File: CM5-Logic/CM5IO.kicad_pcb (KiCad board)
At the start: 4 copper layers, 165 x 165 mm, 129 parts, among them J1 703W-00_53, J10 691210910004, J11 690-019-298-412, J12 USB3_A, J13 JST_SHBM04B-SRSS-TB, J14 Micro_SD_Card_Det, J15 Bus_M.2_Socket_M, J16 SSW-114-01-X-S, J17 SSW-114-01-X-S, J18 6130XX11821_61300811821, J19 6130XX11821_61300811821, J2 B2B-PH-K-S, J20 6130XX11821_61300811821, J21 6130XX11821_61300811821, J3 B2B-PH-K-S, J4 VR10S09, J5 691101810005, J6 691210910006, J7 691210910006, J8 5055750471, J9 1726470103, U1 UWS-5_10-Q48N-C, U10 AP3441SHE-7B, U11 ASEK-32.768KHZ-L-R-T, U12 MAX98357AETE_T, U13 MAX98357AETE_T, U14 CDCLVC1106PWR, U15 CDCLVC1106PWR, U2 RCLAMP3354S.TCT, U3 AP22653W6, U4 RT9742SNGV, U5 74LVC1G07SE-7, U6 TPD4EUSB30, U7 TPD4EUSB30, U8 RT9742GGJ5, U9 MagJack-A70-112-331N126

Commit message: changes USB port, adds TMC2209 SilentStepStick footprint, redoes PCB Layout
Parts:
- removed C35: 10uF, PCM_JLCPCB:C_0402
- removed C36, C37: 100nF, PCM_JLCPCB:C_0402
- removed F1: 4628, Custom Components:FUSE_4628
- removed H1, H2, H3, H4, H5, H6, H7, H8: MountingHole, CM5IO:MountingHole_2.7mm_M2.5_DIN965
- removed J19, J20, J21: 6130XX11821_61300811821, Custom Components:61300811821
- removed MK1, MK2, MK3, MK4, MK5, MK6, MK7, MK8: ICS-43434, Sensor_Audio:InvenSense_ICS-43434-6_3.5x2.65mm
- removed R15, R16, R17, R18, R19, R20: 100Ω, PCM_JLCPCB:R_0603
- removed R21: 2.2kΩ, PCM_JLCPCB:R_0402
- removed R22: 100kΩ, PCM_JLCPCB:R_0402
- removed R23, R24, R25, R26, R27, R28, R29, R30, R31, R32: 33Ω, PCM_JLCPCB:R_0402
- removed U12, U13: MAX98357AETE_T, Custom Components:QFN50P300X300X80-17N
- removed U14, U15: CDCLVC1106PWR, Custom Components:SOP65P640X120-14N
- added PS1: R-78E9.0-0.5, Custom Components:CONV_R-78E9.0-0.5, F.Cu at (535.2, 244.7)
- C10, C24: footprint PCM_JLCPCB:C_0402 -> PCM_JLCPCB:C_0603
- C11, C25, C30: value 100nF -> 10uF; footprint PCM_JLCPCB:C_0402 -> PCM_JLCPCB:C_0805
- C12, C8: value 10uF -> 100nF; footprint PCM_JLCPCB:C_0805 -> PCM_JLCPCB:C_0402
- C13: value 100nF -> 10uF; footprint PCM_JLCPCB:C_0402 -> PCM_JLCPCB:C_0805; moved to B.Cu
- C14, C18, C19, C20, D3, L1, Module1, TP1: moved to B.Cu
- C15, C21: value 10uF -> 100nF; footprint PCM_JLCPCB:C_0805 -> PCM_JLCPCB:C_0402; moved to B.Cu
- C16: value 100nF -> 4.7nF; moved to B.Cu
- C17: value 4.7nF -> 10uF; footprint PCM_JLCPCB:C_0402 -> PCM_JLCPCB:C_0805; moved to B.Cu
- C2: value 22uF -> 10uF; footprint PCM_JLCPCB:C_0805 -> PCM_JLCPCB:C_1206
- C22: value 100nF -> 10uF; footprint PCM_JLCPCB:C_0402 -> PCM_JLCPCB:C_CASE-A-3216-18(mm)
- C23: value WCAP-ASLI_6.3X7.7 -> 100nF; footprint Custom Components:WCAP-ASLI_6.3X7.7_DXL_ -> PCM_JLCPCB:C_0603
- C27: value 100nF -> WCAP-ASLI_6.3X7.7; footprint PCM_JLCPCB:C_0402 -> Custom Components:WCAP-ASLI_6.3X7.7_DXL_
- C3: value WCAP-FTX2_P22.5_CS -> 10uF; footprint Custom Components:WCAP-FTX2_P22.5L26W6H12_CS -> PCM_JLCPCB:C_0805
- C32, C33: value 10uF -> 100nF
- C34: footprint PCM_JLCPCB:C_0402 -> PCM_JLCPCB:C_0805
- C4: value DE1E3RA472MA4BN01F -> 100nF; footprint Custom Components:CAP_DE1E3RA472MA4BN01F -> PCM_JLCPCB:C_CASE-B-3528-21(mm)
- C5: value DE1E3RA472MA4BN01F -> 10uF; footprint Custom Components:CAP_DE1E3RA472MA4BN01F -> PCM_JLCPCB:C_0805
- C7: footprint PCM_JLCPCB:C_CASE-B-3528-21(mm) -> PCM_JLCPCB:C_0402
- C9: footprint PCM_JLCPCB:C_0805 -> PCM_JLCPCB:C_1206
- J1: value 703W-00_53 -> B2B-PH-K-S; footprint Custom Components:QUALTEK_703W-00_53 -> Custom Components:JST_B2B-PH-K-S
- J10: value 691210910004 -> JST_SHBM04B-SRSS-TB; footprint Custom Components:691210910004 -> Connector_JST:JST_SH_BM04B-SRSS-TB_1x04-1MP_P1.00mm_Vertical
- J11: value 690-019-298-412 -> Micro_SD_Card_Det; footprint CM5IO:EDAC 690-019-298-412 -> CM5IO:SDCARD_MOLEX_503398-1892; moved to B.Cu
- J12: value USB3_A -> Bus_M.2_Socket_M; footprint CM5IO:MTCONN_UBAF30-D2011 -> CM5IO:M.2 M Key socket; moved to B.Cu
- J13: value JST_SHBM04B-SRSS-TB -> 6130XX11821_61300811821; footprint Connector_JST:JST_SH_BM04B-SRSS-TB_1x04-1MP_P1.00mm_Vertical -> Custom Components:61300811821
- J14: value Micro_SD_Card_Det -> 6130XX11821_61300811821; footprint CM5IO:SDCARD_MOLEX_503398-1892 -> Custom Components:61300811821
- J15: value Bus_M.2_Socket_M -> SSW-120-01-G-S-LL; footprint CM5IO:M.2 M Key socket -> Custom Components:SAMTEC_SSW-120-01-G-S-LL
- J16: value SSW-114-01-X-S -> SSW-120-01-G-S-LL; footprint Custom Components:SAMTEC_SSW-114-01-X-S -> Custom Components:SAMTEC_SSW-120-01-G-S-LL
- J17: value SSW-114-01-X-S -> 63453-116LF; footprint Custom Components:SAMTEC_SSW-114-01-X-S -> Custom Components:AMPHENOL_63453-116LF
- J18: value 6130XX11821_61300811821 -> 63453-116LF; footprint Custom Components:61300811821 -> Custom Components:AMPHENOL_63453-116LF
- J3: value B2B-PH-K-S -> ED555/4DS; footprint Custom Components:JST_B2B-PH-K-S -> Custom Components:CONN4_ED555&slash_4DS_SHT
- J4: value VR10S09 -> 691210910006; footprint Custom Components:VR10S09 -> Custom Components:691210910006
- J5: value 691101810005 -> 691210910006; footprint Custom Components:691101810005 -> Custom Components:691210910006
- J6: value 691210910006 -> 39291247; footprint Custom Components:691210910006 -> Custom Components:CONN_SD-5569-002_24_MOL
- J7: value 691210910006 -> 39291087; footprint Custom Components:691210910006 -> Custom Components:CONN_SD-5569-002_08_MOL
- J8: value 5055750471 -> 690-019-298-412; footprint Custom Components:MOLEX_5055750471 -> CM5IO:EDAC 690-019-298-412; moved to B.Cu
- J9: value 1726470103 -> 484050003; footprint Custom Components:MOLEX_1726470103 -> Custom Components:484050003_MOL; moved to B.Cu
- R10: value 10kΩ -> 1kΩ; moved to B.Cu
- R11: value 2.2kΩ -> 5.1kΩ; footprint PCM_JLCPCB:R_0402 -> PCM_JLCPCB:R_0603
- R12: value 1kΩ -> 5.1kΩ; footprint PCM_JLCPCB:R_0402 -> PCM_JLCPCB:R_0603
- R13: value 100Ω -> 1MΩ
- R14: value 100Ω -> 470Ω
- R2: value 7.5kΩ -> 1kΩ
- R3: value 7.5kΩ -> 13kΩ; footprint PCM_JLCPCB:R_0402 -> PCM_JLCPCB:R_0805
- R5: value 13kΩ -> 470Ω; footprint PCM_JLCPCB:R_0805 -> PCM_JLCPCB:R_0402
- R6: value 1kΩ -> 470Ω
- R7: value 470Ω -> 100kΩ; moved to B.Cu
- R8: value 470Ω -> 10kΩ; moved to B.Cu
- R9: value 100kΩ -> 2.2kΩ; moved to B.Cu
- U1: value UWS-5_10-Q48N-C -> AP22653W6; footprint Custom Components:VREG_UWS-5_10-Q48N-C -> Package_TO_SOT_SMD:SOT-23-6; moved to F.Cu
- U10: value AP3441SHE-7B -> TMC2209_SILENTSTEPSTICK; footprint Package_DFN_QFN:DFN-8-1EP_2x2mm_P0.5mm_EP1.05x1.75mm -> Custom Components:MODULE_TMC2209_SILENTSTEPSTICK
- U11: value ASEK-32.768KHZ-L-R-T -> PAM8406DR; footprint Crystal:Crystal_SMD_3225-4Pin_3.2x2.5mm -> Custom Components:SO-16_PAM8406_DIO
- U2: value RCLAMP3354S.TCT -> RT9742SNGV; footprint Custom Components:SOT-23-5L_SEM -> Package_TO_SOT_SMD:TSOT-23_HandSoldering
- U3: value AP22653W6 -> 74LVC1G07SE-7; footprint Package_TO_SOT_SMD:SOT-23-6 -> Package_TO_SOT_SMD:SOT-353_SC-70-5
- U4: value RT9742SNGV -> TPD4EUSB30; footprint Package_TO_SOT_SMD:TSOT-23_HandSoldering -> Package_SON:USON-10_2.5x1.0mm_P0.5mm
- U5: value 74LVC1G07SE-7 -> TPD4EUSB30; footprint Package_TO_SOT_SMD:SOT-353_SC-70-5 -> Package_SON:USON-10_2.5x1.0mm_P0.5mm
- U6: value TPD4EUSB30 -> RT9742GGJ5; footprint Package_SON:USON-10_2.5x1.0mm_P0.5mm -> Package_TO_SOT_SMD:SOT-23-5
- U7: value TPD4EUSB30 -> MagJack-A70-112-331N126; footprint Package_SON:USON-10_2.5x1.0mm_P0.5mm -> CM5IO:TRJG0926HENL; moved to B.Cu
- U8: value RT9742GGJ5 -> AP3441SHE-7B; footprint Package_TO_SOT_SMD:SOT-23-5 -> Package_DFN_QFN:DFN-8-1EP_2x2mm_P0.5mm_EP1.05x1.75mm; moved to B.Cu
- U9: value MagJack-A70-112-331N126 -> ASEK-32.768KHZ-L-R-T; footprint CM5IO:TRJG0926HENL -> Crystal:Crystal_SMD_3225-4Pin_3.2x2.5mm; moved to B.Cu
- Ue1: value L9110S -> L9110H
- moved J1 382.3 mm to (335.4, 197.2), turned to 0 degrees
- moved C31 371.9 mm to (360.1, 180.3), turned to 0 degrees
- moved C23 367.4 mm to (290.3, 296.9), turned to 0 degrees
- moved C29 361.1 mm to (360.1, 176.6), turned to 0 degrees
- moved C3 360.3 mm to (328.1, 265.4), turned to 0 degrees
- moved R14 347.8 mm to (286.5, 298.2), turned to 0 degrees
- moved C5 340.1 mm to (328.1, 268.4)
- moved C1 336.1 mm to (334.5, 218.9), turned to 0 degrees
- moved D1 328.8 mm to (347.8, 250.8), turned to 0 degrees
- moved C4 327.0 mm to (340.3, 266.0), turned to 0 degrees
- moved D2 326.8 mm to (347.8, 253.4), turned to 0 degrees
- moved J10 317.7 mm to (372.6, 245.5), turned to 0 degrees
- moved C24 315.5 mm to (290.3, 299.1), turned to 0 degrees
- moved R13 314.8 mm to (286.5, 300.5), turned to 0 degrees
- moved R4 311.5 mm to (366.8, 247.0), turned to 0 degrees
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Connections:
- C1 pad 1: GND -> /+12v
- C1 pad 2: /+24v -> GND
- C11 pad 1: /CM5_HighSpeed/HDMI_5v -> /CM5_GPIO ( Ethernet, GPIO, SDCARD)/SD_PWR
- C12 pad 1: /CM5_GPIO ( Ethernet, GPIO, SDCARD)/SD_PWR -> Net-(C12-Pad1)
- C13 pad 1: Net-(C13-Pad1) -> /+5v
- C16 pad 1: /+5v -> /PCIe-M2/M2_3v3
- C16 pad 2: GND -> /PCIe-M2/FB
- C17 pad 2: /PCIe-M2/FB -> GND
- C22 pad 1: /PCIe-M2/M2_3v3 -> /+5v
- C23 pad 1: /+24v -> /+5v
- C24 pad 2: /+3.3v_P -> Net-(C24-Pad2)
- C25 pad 2: /+3.3v_P -> /+5v
- C26 pad 2: /+3.3v_P -> /+5v
- C27 pad 1: GND -> /+12v
- C27 pad 2: /+3.3v_P -> GND
- C28 pad 1: GND -> /+5v
- C28 pad 2: /+3.3v_P -> GND
- C29 pad 1: GND -> /+5v
- C29 pad 2: /+3.3v_P -> GND
- C3 pad 1: /AC_neutral2 -> /+5v
- C3 pad 2: /AC_line -> GND
- C30 pad 1: GND -> /+5v
- C30 pad 2: /+3.3v_P -> GND
- C31 pad 1: GND -> Net-(U11-INL)
- C31 pad 2: /+3.3v_P -> /HPL
- C32 pad 1: GND -> /HPR
- C32 pad 2: /+5v -> Net-(U11-INR)
- C33 pad 1: GND -> /+5v
- C33 pad 2: /+5v -> GND
- C34 pad 1: GND -> /+5v
- C34 pad 2: /+5v -> GND
- C4 pad 1: /AC_neutral2 -> /CM5_HighSpeed/VBUS
- C4 pad 2: /AC_Earth -> GND
- C5 pad 1: /AC_Earth -> /CM5_HighSpeed/VBUS
- C5 pad 2: /AC_line -> GND
- C6 pad 1: /+5v -> /CM5_HighSpeed/VBUS
- C7 pad 1: /CM5_HighSpeed/VBUS -> /+5v
- C8 pad 1: /CM5_HighSpeed/VBUS -> /CM5_HighSpeed/HDMI_5v
- C9 pad 1: /CM5_HighSpeed/VBUS -> /+5v
- D1 pad 2: /+3.3v_P -> /CM5_GPIO ( Ethernet, GPIO, SDCARD)/+3.3v_P
- D2 pad 2: /+3.3v_P -> /CM5_GPIO ( Ethernet, GPIO, SDCARD)/+3.3v_P
- J1 pad 1: /AC_neutral1 -> /PAM8406DR_Amp/OUT_R+
- J1 pad 2: /AC_Earth -> /PAM8406DR_Amp/OUT_R-
- J10 pad 1: /DRV225/S_B2 -> /+5v
- J10 pad 2: /DRV225/S_B1 -> /CM5_GPIO ( Ethernet, GPIO, SDCARD)/PWM
- J10 pad 3: /DRV225/S_A1 -> GND
- J10 pad 4: /DRV225/S_A2 -> /CM5_GPIO ( Ethernet, GPIO, SDCARD)/TACHO
- J11 pad 1: /CM5_HighSpeed/HDMI0_D2_P -> /CM5_GPIO ( Ethernet, GPIO, SDCARD)/SD_DAT2
- J11 pad 10: /CM5_HighSpeed/HDMI0_CK_P -> unconnected-(J11-DET_A-Pad10)
- J11 pad 2: GND -> /CM5_GPIO ( Ethernet, GPIO, SDCARD)/SD_DAT3
- J11 pad 3: /CM5_HighSpeed/HDMI0_D2_N -> /CM5_GPIO ( Ethernet, GPIO, SDCARD)/SD_CMD
- J11 pad 4: /CM5_HighSpeed/HDMI0_D1_P -> /CM5_GPIO ( Ethernet, GPIO, SDCARD)/SD_PWR
- J11 pad 5: GND -> /CM5_GPIO ( Ethernet, GPIO, SDCARD)/SD_CLK
- J11 pad 6: /CM5_HighSpeed/HDMI0_D1_N -> GND
- J11 pad 7: /CM5_HighSpeed/HDMI0_D0_P -> /CM5_GPIO ( Ethernet, GPIO, SDCARD)/SD_DAT0
- J11 pad 8: GND -> /CM5_GPIO ( Ethernet, GPIO, SDCARD)/SD_DAT1
- J11 pad 9: /CM5_HighSpeed/HDMI0_D0_N -> unconnected-(J11-DET_B-Pad9)
- J12 pad 10: GND -> Net-(J12-DAS/~{DSS}/~{LED1})
- J13 pad 1: /+5v -> GND
- J13 pad 2: /CM5_GPIO ( Ethernet, GPIO, SDCARD)/PWM -> GND
- J13 pad 4: /CM5_GPIO ( Ethernet, GPIO, SDCARD)/TACHO -> /+3.3v_ESP32
- J14 pad 1: /CM5_GPIO ( Ethernet, GPIO, SDCARD)/SD_DAT2 -> GND
- J14 pad 2: /CM5_GPIO ( Ethernet, GPIO, SDCARD)/SD_DAT3 -> /+3.3v_ESP32
- J14 pad 3: /CM5_GPIO ( Ethernet, GPIO, SDCARD)/SD_CMD -> /BNO086/SCK
- J14 pad 4: /CM5_GPIO ( Ethernet, GPIO, SDCARD)/SD_PWR -> /BNO086/SO
- J14 pad 5: /CM5_GPIO ( Ethernet, GPIO, SDCARD)/SD_CLK -> /BNO086/SI
- J14 pad 6: GND -> /BNO086/CS
- J14 pad 7: /CM5_GPIO ( Ethernet, GPIO, SDCARD)/SD_DAT0 -> /BNO086/WAK
- J14 pad 8: /CM5_GPIO ( Ethernet, GPIO, SDCARD)/SD_DAT1 -> unconnected-(J14-Pad8)
- J15 pad 10: Net-(J15-DAS/~{DSS}/~{LED1}) -> unconnected-(J15-Pad10)
- J15 pad 12: /PCIe-M2/M2_3v3 -> unconnected-(J15-Pad12)
- J15 pad 13: unconnected-(J15-PERp3-Pad13) -> /n_IA
- J15 pad 14: /PCIe-M2/M2_3v3 -> /n_IB
- J15 pad 15: GND -> /n_SenseSCL
- J15 pad 16: /PCIe-M2/M2_3v3 -> /n_SenseSDA
- J15 pad 17: unconnected-(J15-PETn2-Pad17) -> /n_RST
- J15 pad 18: /PCIe-M2/M2_3v3 -> /n_INT
- J15 pad 19: unconnected-(J15-PETp2-Pad19) -> /+5v
- J15 pad 20: unconnected-(J15-NC-Pad20) -> GND
- J16 pad 02: /Teensy_4.0_Harness/0 -> unconnected-(J16-Pad02)
- J16 pad 03: /T_IA -> /n_UART
- J16 pad 04: /T_IB -> Net-(C24-Pad2)
- J16 pad 05: /Teensy_4.0_Harness/3 -> /T
- J16 pad 06: /Teensy_4.0_Harness/4 -> unconnected-(J16-Pad06)
- J16 pad 07: /DRV225/T_Step -> unconnected-(J16-Pad07)
- J16 pad 08: /DRV225/T_Dir -> unconnected-(J16-Pad08)
- J16 pad 09: /DRV225/T_EN -> unconnected-(J16-Pad09)
- J16 pad 10: /DRV225/T_M0 -> unconnected-(J16-Pad10)
- J16 pad 11: /DRV225/T_M1 -> unconnected-(J16-Pad11)
- J16 pad 12: /DRV225/T_M2 -> unconnected-(J16-Pad12)
- J16 pad 13: /T_RST -> unconnected-(J16-Pad13)
- J16 pad 14: /T_INT -> /n_AB
- J17 pad 01: /Teensy_4.0_Harness/13 -> unconnected-(J17-Pad01)
- J17 pad 02: /T_A0 -> unconnected-(J17-Pad02)
- J17 pad 03: /Teensy_4.0_Harness/15 -> unconnected-(J17-Pad03)
- J17 pad 04: /T_SenseSCL -> unconnected-(J17-Pad04)
- J17 pad 05: /T_SenseSDA -> unconnected-(J17-Pad05)
- J17 pad 06: /T_BotSDA -> unconnected-(J17-Pad06)
- J17 pad 07: /T_BotSCL -> unconnected-(J17-Pad07)
- J17 pad 08: /Teensy_4.0_Harness/20 -> unconnected-(J17-Pad08)
- J17 pad 09: /T_AB -> unconnected-(J17-Pad09)
- J17 pad 10: /T_AG -> unconnected-(J17-Pad10)
- J17 pad 11: /T_AR -> unconnected-(J17-Pad11)
- J17 pad 12: /+3.3v_T -> unconnected-(J17-Pad12)
- J17 pad 13: GND -> /USB2-D_P
- J17 pad 14: /+5v -> unconnected-(J17-Pad14)
- J2 pad 1: /MaxAmplifier/OUTPL -> /PAM8406DR_Amp/OUT_L+
- J2 pad 2: /MaxAmplifier/OUTNL -> /PAM8406DR_Amp/OUT_L-
- J3 pad 1: /MaxAmplifier/OUTPR -> /TMC2209/B2
- J3 pad 2: /MaxAmplifier/OUTNR -> /TMC2209/B1
- J4 pad 1: /+24v -> Net-(Ue1-OA)
- J4 pad 2: GND -> Net-(Ue1-OB)
- J4 pad 3: /+9v -> /T
- J5 pad 1: /+24v -> /PWR_BUT
- J5 pad 3: /AC_Earth -> /+3.3v_ESP32
- J5 pad 4: /AC_line -> /n_AR
- J5 pad 5: /AC_neutral2 -> /n_AG
- J6 pad 1: Net-(Ue1-OA) -> unconnected-(J6-Pad1)
- J6 pad 2: Net-(Ue1-OB) -> /+12v
- J6 pad 3: unconnected-(J6-Pad3) -> /+12v
- J6 pad 4: GND -> unconnected-(J6-Pad4)
- J6 pad 5: /T_A0 -> unconnected-(J6-Pad5)
- J6 pad 6: /+3.3v_T -> GND
- J7 pad 1: /PWR_BUT -> GND
- J7 pad 3: /+3.3v_T -> GND
- J7 pad 4: /T_AR -> GND
- J7 pad 5: /T_AG -> /+12v
- J7 pad 6: /T_AB -> /+12v
- J8 pad 1: /T_BotSCL -> /CM5_HighSpeed/HDMI0_D2_P
- J8 pad 2: /T_BotSDA -> GND
- J8 pad 3: /D+ -> /CM5_HighSpeed/HDMI0_D2_N
- J8 pad 4: /D- -> /CM5_HighSpeed/HDMI0_D1_P
- J9 pad 1: GND -> /CM5_HighSpeed/VBUS
- J9 pad 2: /+5v -> /CM5_HighSpeed/USB3-0-D_N
- J9 pad 3: /+24v -> /CM5_HighSpeed/USB3-0-D_P
- L1 pad 1: Net-(U10-LX) -> Net-(U8-LX)
- Module1 pad 103: /D- -> /USB2-D_N
- Module1 pad 105: /D+ -> /USB2-D_P
- Module1 pad 163: /CM5_HighSpeed/USB3-1-D_P -> /USB3_1-D_P
- Module1 pad 165: /CM5_HighSpeed/USB3-1-D_N -> /USB3-1-D_N
- Module1 pad 24: /SDI3 -> unconnected-(Module1A-GPIO26-Pad24)
- Module1 pad 25: /SDO0 -> unconnected-(Module1A-GPIO21-Pad25)
- Module1 pad 26: /WS -> unconnected-(Module1A-GPIO19-Pad26)
- Module1 pad 27: /SDI0 -> unconnected-(Module1A-GPIO20-Pad27)
- Module1 pad 45: /SDI2 -> unconnected-(Module1A-GPIO24-Pad45)
- Module1 pad 46: /SDI1 -> unconnected-(Module1A-GPIO22-Pad46)
- Module1 pad 49: /SCLK -> unconnected-(Module1A-GPIO18-Pad49)
- Module1 pad 56: /T_BotSCL -> unconnected-(Module1A-GPIO3-Pad56)
- Module1 pad 58: /T_BotSDA -> unconnected-(Module1A-GPIO2-Pad58)
- Module1 pad 78: /+3.3v_P -> /CM5_GPIO ( Ethernet, GPIO, SDCARD)/+3.3v_P
- Module1 pad 84: /+3.3v_P -> /CM5_GPIO ( Ethernet, GPIO, SDCARD)/+3.3v_P
- Module1 pad 86: /+3.3v_P -> /CM5_GPIO ( Ethernet, GPIO, SDCARD)/+3.3v_P
- R1 pad 1: Net-(U3-ILIM) -> Net-(U1-ILIM)
- R10 pad 1: /PCIe-M2/M2_3v3 -> Net-(D3-K)
- R10 pad 2: /PCIe-M2/FB -> Net-(J12-DAS/~{DSS}/~{LED1})
- R11 pad 1: /PCIe-M2/FB -> /+3.3v_ESP32
- R11 pad 2: GND -> /n_RST
- R12 pad 1: Net-(D3-K) -> /n_INT
- R12 pad 2: Net-(J15-DAS/~{DSS}/~{LED1}) -> /+3.3v_ESP32
- R13 pad 1: /SDI0 -> /T
- R14 pad 1: /SDI0 -> Net-(C24-Pad2)
- R14 pad 2: GND -> /n_A0
- R2 pad 1: /+3.3v_P -> Net-(D1-K)
- R2 pad 2: /T_BotSCL -> Net-(Module1A-LED_nACT)
- R3 pad 1: /T_BotSDA -> /CM5_GPIO ( Ethernet, GPIO, SDCARD)/SD_PWR_ON
- R3 pad 2: /+3.3v_P -> /CM5_GPIO ( Ethernet, GPIO, SDCARD)/+3.3v_P
- R4 pad 1: Net-(D1-K) -> Net-(D2-K)
- R4 pad 2: Net-(Module1A-LED_nACT) -> Net-(R4-Pad2)
- R5 pad 1: /CM5_GPIO ( Ethernet, GPIO, SDCARD)/SD_PWR_ON -> /CM5_GPIO ( Ethernet, GPIO, SDCARD)/ETH_LEDG
- R5 pad 2: /+3.3v_P -> Net-(U7-LEDY_K)
- R6 pad 1: Net-(D2-K) -> /CM5_GPIO ( Ethernet, GPIO, SDCARD)/ETH_LEDY
- R6 pad 2: Net-(R6-Pad2) -> Net-(U7-LEDG_K)
- R7 pad 1: /CM5_GPIO ( Ethernet, GPIO, SDCARD)/ETH_LEDG -> /CM5_HighSpeed/PCIE_PWR_EN
- R7 pad 2: Net-(U9-LEDY_K) -> GND
- R8 pad 1: /CM5_GPIO ( Ethernet, GPIO, SDCARD)/ETH_LEDY -> /PCIe-M2/M2_3v3
- R8 pad 2: Net-(U9-LEDG_K) -> /PCIe-M2/FB
- R9 pad 1: /CM5_HighSpeed/PCIE_PWR_EN -> /PCIe-M2/FB
- U1 pad 1: /+24v -> /+5v
- U1 pad 3: GND -> /CM5_HighSpeed/VBUS_EN
- U1 pad 4: GND -> unconnected-(U1-nFault-Pad4)
- U1 pad 5: GND -> Net-(U1-ILIM)
- U1 pad 6: unconnected-(U1-TRIM-Pad6) -> /CM5_HighSpeed/VBUS
- U10 pad 1: /PCIe-M2/FB -> GND
- U10 pad 2: unconnected-(U10-PG-Pad2) -> /+3.3v_ESP32
- U10 pad 3: /+5v -> /TMC2209/B1
- U10 pad 4: GND -> /TMC2209/A2
- U10 pad 5: unconnected-(U10-nc-Pad5) -> /TMC2209/A1
- U10 pad 6: Net-(U10-LX) -> /TMC2209/B2
- U10 pad 7: /CM5_HighSpeed/PCIE_PWR_EN -> GND
- U10 pad 8: GND -> /+12v
- U10 pad 9: GND -> /n_Dir
- U11 pad 1: /PCIe-M2/M2_3v3 -> /PAM8406DR_Amp/OUT_L+
- U11 pad 3: Net-(J15-SUSCLK) -> /PAM8406DR_Amp/OUT_L-
- U11 pad 4: /PCIe-M2/M2_3v3 -> /+5v
- U2 pad 1: /T_BotSCL -> /+5v
- U2 pad 2: GND -> /CM5_HighSpeed/HDMI_5v
- U2 pad 3: /D- -> GND
- U3 pad 1: /+5v -> unconnected-(U3-nc-Pad1)
- U3 pad 2: GND -> /CM5_GPIO ( Ethernet, GPIO, SDCARD)/nPWR_LED
- U3 pad 3: /CM5_HighSpeed/VBUS_EN -> GND
- U3 pad 4: unconnected-(U3-nFault-Pad4) -> Net-(R4-Pad2)
- U3 pad 5: Net-(U3-ILIM) -> /CM5_GPIO ( Ethernet, GPIO, SDCARD)/+3.3v_P
- U4 pad 1: /+5v -> /CM5_GPIO ( Ethernet, GPIO, SDCARD)/TRD3_P
- U4 pad 2: /CM5_HighSpeed/HDMI_5v -> /CM5_GPIO ( Ethernet, GPIO, SDCARD)/TRD3_N
- U5 pad 1: unconnected-(U5-nc-Pad1) -> /CM5_GPIO ( Ethernet, GPIO, SDCARD)/TRD1_P
- U5 pad 2: /CM5_GPIO ( Ethernet, GPIO, SDCARD)/nPWR_LED -> /CM5_GPIO ( Ethernet, GPIO, SDCARD)/TRD1_N
- U5 pad 4: Net-(R6-Pad2) -> /CM5_GPIO ( Ethernet, GPIO, SDCARD)/TRD0_N
- U5 pad 5: /+3.3v_P -> /CM5_GPIO ( Ethernet, GPIO, SDCARD)/TRD0_P
- U6 pad 1: /CM5_GPIO ( Ethernet, GPIO, SDCARD)/TRD3_P -> /CM5_GPIO ( Ethernet, GPIO, SDCARD)/SD_PWR
- U6 pad 2: /CM5_GPIO ( Ethernet, GPIO, SDCARD)/TRD3_N -> GND
- U6 pad 3: GND -> unconnected-(U6-nFLG-Pad3)
- U6 pad 4: /CM5_GPIO ( Ethernet, GPIO, SDCARD)/TRD2_N -> /CM5_GPIO ( Ethernet, GPIO, SDCARD)/SD_PWR_ON
- U6 pad 5: /CM5_GPIO ( Ethernet, GPIO, SDCARD)/TRD2_P -> /CM5_GPIO ( Ethernet, GPIO, SDCARD)/+3.3v_P
- U7 pad 1: /CM5_GPIO ( Ethernet, GPIO, SDCARD)/TRD1_P -> /CM5_GPIO ( Ethernet, GPIO, SDCARD)/TRD0_P
- U7 pad 10: /CM5_GPIO ( Ethernet, GPIO, SDCARD)/TRD1_P -> /CM5_GPIO ( Ethernet, GPIO, SDCARD)/TRD3_N
- U7 pad 2: /CM5_GPIO ( Ethernet, GPIO, SDCARD)/TRD1_N -> /CM5_GPIO ( Ethernet, GPIO, SDCARD)/TRD0_N
- U7 pad 3: GND -> /CM5_GPIO ( Ethernet, GPIO, SDCARD)/TRD1_P
- U7 pad 4: /CM5_GPIO ( Ethernet, GPIO, SDCARD)/TRD0_N -> Net-(C12-Pad1)
- U7 pad 5: /CM5_GPIO ( Ethernet, GPIO, SDCARD)/TRD0_P -> Net-(C12-Pad1)
- U7 pad 6: /CM5_GPIO ( Ethernet, GPIO, SDCARD)/TRD0_P -> /CM5_GPIO ( Ethernet, GPIO, SDCARD)/TRD1_N
- U7 pad 7: /CM5_GPIO ( Ethernet, GPIO, SDCARD)/TRD0_N -> /CM5_GPIO ( Ethernet, GPIO, SDCARD)/TRD2_P
- U7 pad 8: GND -> /CM5_GPIO ( Ethernet, GPIO, SDCARD)/TRD2_N
- U7 pad 9: /CM5_GPIO ( Ethernet, GPIO, SDCARD)/TRD1_N -> /CM5_GPIO ( Ethernet, GPIO, SDCARD)/TRD3_P
- U8 pad 1: /CM5_GPIO ( Ethernet, GPIO, SDCARD)/SD_PWR -> /PCIe-M2/FB
- U8 pad 2: GND -> unconnected-(U8-PG-Pad2)
- U8 pad 3: unconnected-(U8-nFLG-Pad3) -> /+5v
- U8 pad 4: /CM5_GPIO ( Ethernet, GPIO, SDCARD)/SD_PWR_ON -> GND
- U8 pad 5: /+3.3v_P -> unconnected-(U8-nc-Pad5)
- U9 pad 1: /CM5_GPIO ( Ethernet, GPIO, SDCARD)/TRD0_P -> /PCIe-M2/M2_3v3
- U9 pad 2: /CM5_GPIO ( Ethernet, GPIO, SDCARD)/TRD0_N -> GND
- U9 pad 3: /CM5_GPIO ( Ethernet, GPIO, SDCARD)/TRD1_P -> Net-(J12-SUSCLK)
- U9 pad 4: Net-(C13-Pad1) -> /PCIe-M2/M2_3v3
- Ue1 pad 6: /T_IA -> /n_IA
- Ue1 pad 7: /T_IB -> /n_IB
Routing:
- net /WS: track 719.2 -> 0.00 mm, vias 8 -> 0
- net /SCLK: track 712.9 -> 0.00 mm, vias 10 -> 0
- net /+3.3v_P: track 547.2 -> 0.00 mm, vias 21 -> 0
- net /+5v: track 463.2 -> 0.00 mm, vias 13 -> 0
- net /SDI1: track 241.0 -> 0.00 mm
- net /SDI2: track 236.7 -> 0.00 mm, vias 3 -> 0
- net GND: track 227.6 -> 0.00 mm, vias 84 -> 0
- net /SDI3: track 220.9 -> 0.00 mm, vias 5 -> 0
- net /AC_neutral2: track 208.4 -> 0.00 mm
- net /+24v: track 163.1 -> 0.00 mm, vias 1 -> 0
- net /AC_line: track 139.4 -> 0.00 mm
- net /+3.3v_T: track 136.7 -> 0.00 mm
- net /CM5_GPIO ( Ethernet, GPIO, SDCARD)/TRD3_N: track 130.1 -> 0.00 mm, vias 2 -> 0
- net /CM5_GPIO ( Ethernet, GPIO, SDCARD)/TRD3_P: track 130.0 -> 0.00 mm, vias 2 -> 0
- net /CM5_GPIO ( Ethernet, GPIO, SDCARD)/TRD2_N: track 126.5 -> 0.00 mm, vias 3 -> 0
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- removed copper zone on F.Cu, net /+5v
- removed copper zone on B.Cu, net /CM5_HighSpeed/VBUS
- removed copper zone on F.Cu, net /PCIe-M2/M2_3v3
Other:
- outline, holes or cut-outs redrawn

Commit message: Finishes PCB Pad Layout, Updates LED Status Circuit to RPI Foundations newest version
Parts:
- removed U3: 74LVC1G07SE-7, Package_TO_SOT_SMD:SOT-353_SC-70-5
- added R15: 10kΩ, PCM_JLCPCB:R_0402, F.Cu at (267.0, 321.2)
- C1, C10, C11, C12, C22, C23, C24, C3, C4, C5, C6, C7, C8, C9, D1, D2, J10, R1, R14, R2, R3, R4, R5, R6, U1, U2, U4, U5, U6: moved to B.Cu
- TP1: moved to F.Cu
- moved C35 288.2 mm to (259.5, 265.0), turned to 90 degrees
- moved J9 271.9 mm to (225.0, 362.0)
- moved U7 271.9 mm to (201.6, 364.9)
- moved J11 271.9 mm to (261.5, 368.8)
- moved J8 271.9 mm to (241.6, 366.5)
- moved J3 270.7 mm to (294.3, 248.7)
- moved J12 270.3 mm to (164.9, 332.0)
- moved J5 269.0 mm to (298.7, 259.1)
- moved TP1 268.3 mm to (151.5, 331.7)
- moved J13 267.7 mm to (304.9, 351.0)
- moved J14 267.7 mm to (282.0, 351.0)
- moved D3 267.6 mm to (152.2, 327.4), turned to 90 degrees
- moved J4 267.5 mm to (298.7, 270.1)
- moved C2 267.1 mm to (264.5, 280.4)
- moved J16 266.8 mm to (305.2, 280.2)
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- renumbered C27 to C35, U11 to U10, U10 to U11
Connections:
- J3 pad 2: /TMC2209/B1 -> /TMC2209/A1
- J3 pad 3: /TMC2209/A1 -> /TMC2209/A2
- J3 pad 4: /TMC2209/A2 -> /TMC2209/B1
- J4 pad 1: Net-(Ue1-OA) -> Net-(Ue1-OB)
- J4 pad 2: Net-(Ue1-OB) -> Net-(Ue1-OA)
- R4 pad 2: Net-(R4-Pad2) -> /CM5_GPIO ( Ethernet, GPIO, SDCARD)/nPWR_LED

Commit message: Routes and tunes ethernet/hdmi
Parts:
- moved C17 121.3 mm to (285.9, 388.9)
- moved C18 121.3 mm to (285.9, 387.2)
- moved C19 121.3 mm to (285.9, 385.4)
- moved C20 121.3 mm to (285.9, 383.7)
- moved C24 121.3 mm to (414.6, 343.6)
- moved C5 121.3 mm to (334.2, 413.1)
- moved C6 121.3 mm to (334.2, 414.8)
- moved D2 121.3 mm to (382.3, 431.4)
- moved D3 121.3 mm to (259.4, 384.2)
- moved J11 121.3 mm to (368.7, 425.6)
- moved J16 121.3 mm to (412.4, 336.9)
- moved R10 121.3 mm to (259.4, 386.4)
- moved R2 121.3 mm to (380.6, 429.4)
- moved R4 121.3 mm to (383.9, 429.4)
- moved U10 121.3 mm to (398.8, 292.5)
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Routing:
- net /CM5_HighSpeed/HDMI0_CK_N: track 0.00 -> 23.5 mm
- net /CM5_HighSpeed/HDMI0_CK_P: track 0.00 -> 23.5 mm
- net /CM5_HighSpeed/HDMI0_D1_N: track 0.00 -> 23.4 mm
- net /CM5_HighSpeed/HDMI0_D2_N: track 0.00 -> 23.4 mm
- net /CM5_HighSpeed/HDMI0_D0_P: track 0.00 -> 23.1 mm
- net /CM5_HighSpeed/HDMI0_D0_N: track 0.00 -> 23.1 mm
- net /CM5_HighSpeed/HDMI0_D1_P: track 0.00 -> 22.7 mm
- net /CM5_HighSpeed/HDMI0_D2_P: track 0.00 -> 22.6 mm
- net /CM5_GPIO ( Ethernet, GPIO, SDCARD)/TRD1_N: track 0.00 -> 9.17 mm
- net /CM5_GPIO ( Ethernet, GPIO, SDCARD)/TRD1_P: track 0.00 -> 9.05 mm
- net /CM5_GPIO ( Ethernet, GPIO, SDCARD)/TRD3_N: track 0.00 -> 7.43 mm
- net Net-(C12-Pad1): track 0.00 -> 6.51 mm
- net /CM5_GPIO ( Ethernet, GPIO, SDCARD)/TRD2_N: track 0.00 -> 5.84 mm
- net /CM5_GPIO ( Ethernet, GPIO, SDCARD)/TRD0_N: track 0.00 -> 5.77 mm
- net /CM5_GPIO ( Ethernet, GPIO, SDCARD)/TRD0_P: track 0.00 -> 5.52 mm
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
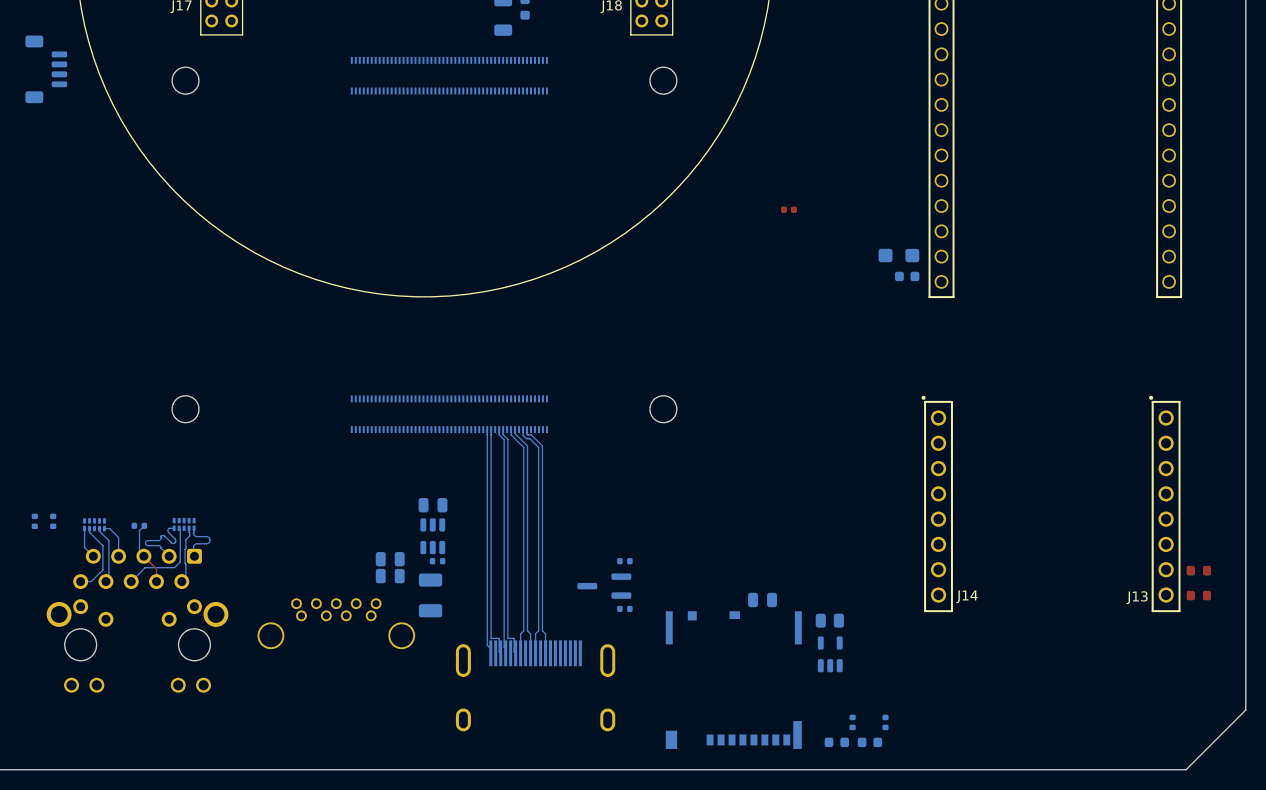
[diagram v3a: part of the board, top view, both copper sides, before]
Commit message: Routes and tunes most of the debug interface, upadtes 3D models
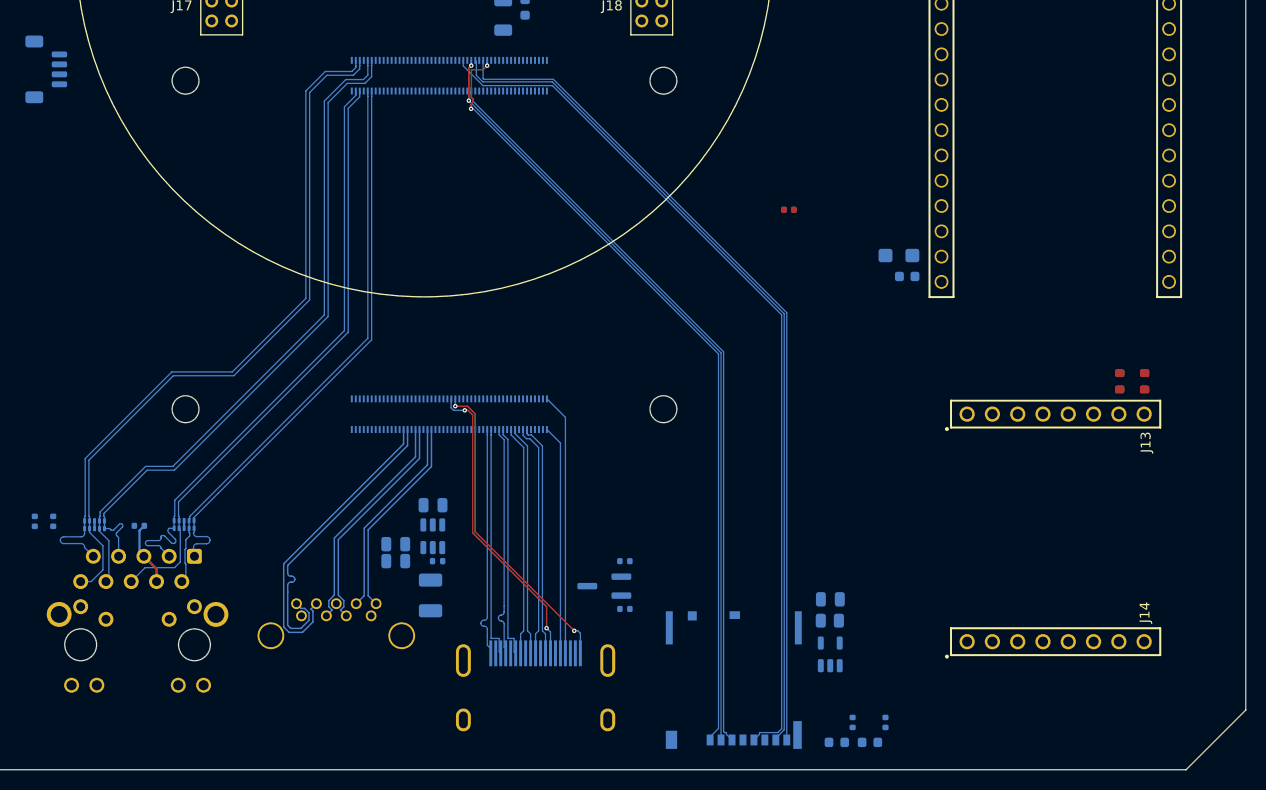
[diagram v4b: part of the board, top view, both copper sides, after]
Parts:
- moved R12 22.2 mm to (409.9, 395.2), turned to 90 degrees
- moved R11 20.6 mm to (407.4, 395.2), turned to -90 degrees
- moved J14 18.0 mm to (401.0, 421.3), turned to 0 degrees
- moved J13 14.5 mm to (401.0, 398.5), turned to 0 degrees
- moved C11 6.81 mm to (378.4, 417.1)
- moved C5 1.61 mm to (334.7, 411.5)
- moved C6 1.61 mm to (334.7, 413.2)
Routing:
- net /CM5_GPIO ( Ethernet, GPIO, SDCARD)/SD_CLK: track 0.00 -> 87.8 mm
- net /CM5_GPIO ( Ethernet, GPIO, SDCARD)/SD_DAT0: track 0.00 -> 85.6 mm
- net /CM5_GPIO ( Ethernet, GPIO, SDCARD)/SD_DAT1: track 0.00 -> 85.0 mm
- net /CM5_GPIO ( Ethernet, GPIO, SDCARD)/SD_DAT2: track 0.00 -> 80.5 mm, vias 0 -> 2
- net /CM5_GPIO ( Ethernet, GPIO, SDCARD)/SD_DAT3: track 0.00 -> 78.9 mm, vias 0 -> 2
- net /CM5_GPIO ( Ethernet, GPIO, SDCARD)/SD_CMD: track 0.00 -> 76.1 mm
- net /CM5_GPIO ( Ethernet, GPIO, SDCARD)/TRD3_P: track 3.15 -> 70.8 mm
- net /CM5_GPIO ( Ethernet, GPIO, SDCARD)/TRD3_N: track 7.43 -> 70.9 mm
- net /CM5_GPIO ( Ethernet, GPIO, SDCARD)/TRD2_P: track 3.68 -> 66.5 mm
- net /CM5_GPIO ( Ethernet, GPIO, SDCARD)/TRD2_N: track 5.84 -> 66.7 mm
- net /CM5_GPIO ( Ethernet, GPIO, SDCARD)/TRD1_N: track 9.17 -> 60.7 mm
- net /CM5_GPIO ( Ethernet, GPIO, SDCARD)/TRD1_P: track 9.05 -> 60.5 mm
- net /CM5_GPIO ( Ethernet, GPIO, SDCARD)/TRD0_N: track 5.77 -> 57.1 mm
- net /CM5_GPIO ( Ethernet, GPIO, SDCARD)/TRD0_P: track 5.52 -> 56.9 mm
- net /CM5_HighSpeed/HDMI0_HOTPLUG: track 0.00 -> 31.7 mm, vias 0 -> 2
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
